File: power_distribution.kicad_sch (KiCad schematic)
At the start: 79 parts, among them Q1 PMOS, Q10 2PNP, Q11 2NPN, Q12 PMOS, Q13 2PNP, Q14 2PNP, Q15 2PNP, Q2 PMOS, Q3 2NPN, Q4 PMOS, Q5 PMOS, Q6 PMOS, Q7 PMOS, Q8 2NPN, Q9 PMOS, U1 PAC1954

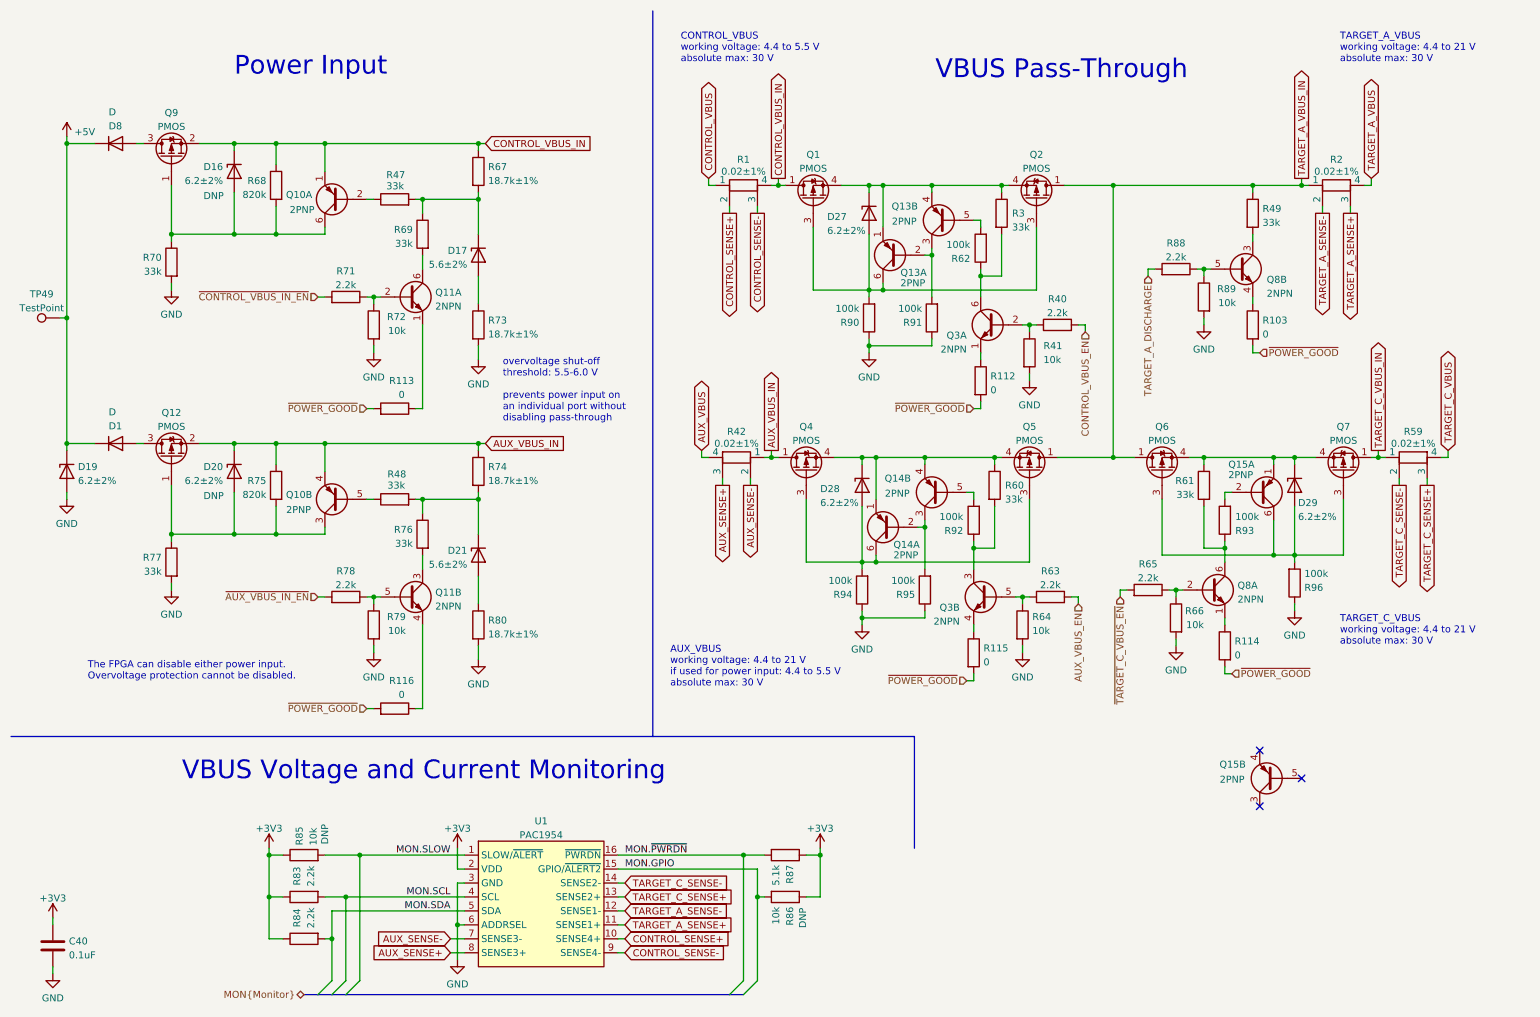
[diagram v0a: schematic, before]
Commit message: Change TARGET_C_VBUS pass-through default
Previously pass-through power between TARGET C and TARGET A was enabled
by default, even when the Cynthion was unpowered. This had the potential
benefit of allowing a pass-through target device to function while the
Cynthion was off, but the feature was unreliable due to loading of D+/D-
by the PHY and TARGET_FS_MONITOR connections. All pass-through power is
now disabled by default, providing a consistent user experience while
the Cynthion is unpowered.
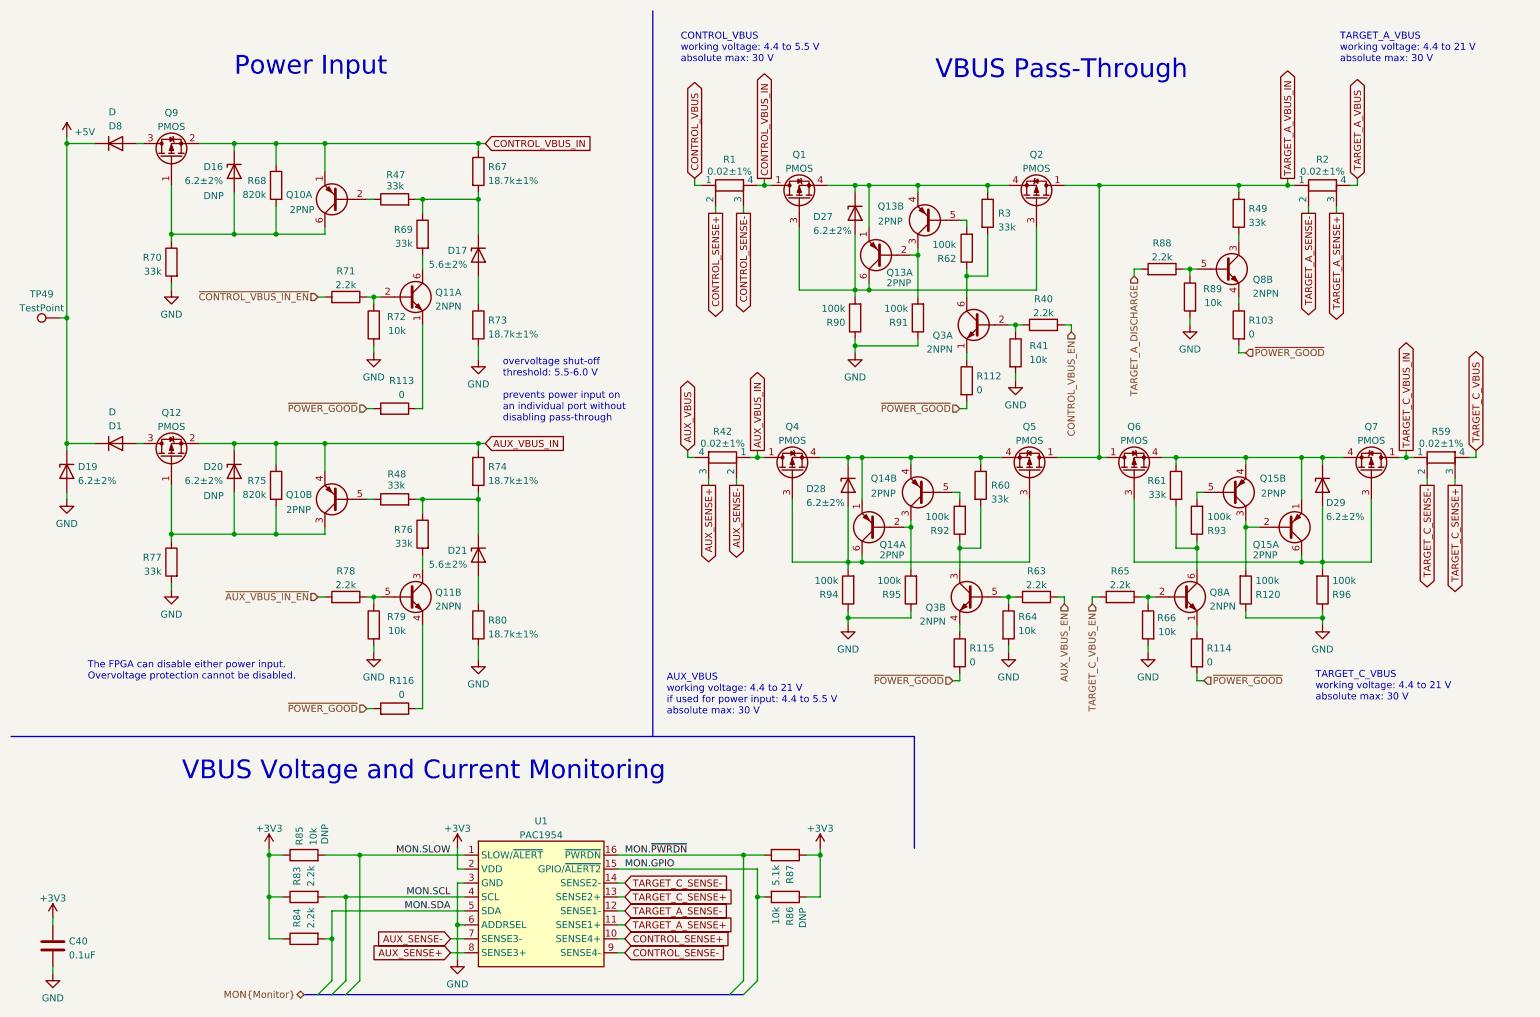
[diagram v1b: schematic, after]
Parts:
- added R120: 100k, Resistor_SMD:R_0402_1005Metric, symbol Device:R
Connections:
- net GND: now also R120.1
- net at D29.1 (K), Q15.1 (E1), Q6.4 (S)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: now also Q15.4 (E2)
- net at Q15.3 (C2): now also Q15.2 (B1), R120.2
- net at Q15.5 (B2): now also R93.2
- net ~{TARGET_C_VBUS_EN} renamed TARGET_C_VBUS_EN
- no-connect marks 3 -> 0
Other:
- moved on the sheet: D27, D28, D29, Q1, Q13A, Q13B, Q14A, Q14B, Q15A, Q15B, Q3A, Q3B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

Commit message: Update copyright notices
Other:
- company: Copyright 2019-2023 Great Scott Gadgets -> ${COPYRIGHT}
- title: Cynthion -> ${TITLE}
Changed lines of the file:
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@@
   (paper "A4")
   (title_block
-    (title "Cynthion")
+    (title "${TITLE}")
     (date "${DATE}")
     (rev "${VERSION}")
-    (company "Copyright 2019-2023 Great Scott Gadgets")
-    (comment 1 "Licensed under the CERN-OHL-P v2")
+    (company "${COPYRIGHT}")
+    (comment 1 "${LICENSE}")
   )
   (bus_alias "Monitor" (members "SDA" "SCL" "SLOW" "GPIO" "~{PWRDN}"))
